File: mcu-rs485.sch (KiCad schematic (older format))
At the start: 10 parts

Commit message: Initial PCB routed
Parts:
- removed U?: ATmega2560-16AU, Package_QFP:TQFP-100_14x14mm_P0.5mm, symbol MCU_Microchip_ATmega:ATmega2560-16AU
- added C46, C8: 100uF, Capacitor_SMD:CP_Elec_6.3x5.4, symbol Device:CP
- added C47, C53, C54, C55: 100nF, Capacitor_SMD:C_0603_1608Metric_Pad1.08x0.95mm_HandSolder, symbol Device:C_Small
- added F1: Fuse, Fuse:Fuse_1206_3216Metric_Pad1.42x1.75mm_HandSolder, symbol Device:Fuse
- added U10, U11, U12: MCP23S17_SS, Package_SO:SSOP-28_5.3x10.2mm_P0.65mm, symbol Interface_Expansion:MCP23S17_SS
- added U6: TSOP382xx, OptoDevice:Vishay_MINICAST-3Pin, symbol Interface_Optical:TSOP382xx
- added U9: ATmega328PB-AU, Package_QFP:TQFP-32_7x7mm_P0.8mm, symbol MCU_Microchip_ATmega:ATmega328PB-AU
- C48, C51, C52: renamed from C?; footprint (none) -> Capacitor_SMD:C_0603_1608Metric_Pad1.08x0.95mm_HandSolder
- C49, C50: renamed from C?; footprint (none) -> Capacitor_SMD:C_0805_2012Metric_Pad1.18x1.45mm_HandSolder
- J1: renamed from J?; footprint (none) -> Connector_Dsub:DSUB-9_Female_Horizontal_P2.77x2.84mm_EdgePinOffset9.90mm_Housed_MountingHolesOffset11.32mm
- R53: renamed from R?; footprint (none) -> Resistor_SMD:R_0603_1608Metric_Pad0.98x0.95mm_HandSolder
- U8: renamed from U?; footprint (none) -> Package_SO:SO-8_5.3x6.2mm_P1.27mm
- Y1: renamed from Y?; footprint (none) -> Crystal:Resonator_SMD_muRata_CSTxExxV-3Pin_3.0x1.1mm_HandSoldering
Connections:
- net labels added: IR_OUT, MISO, MOSI, SCK, SS0, SS1, SS2
- wire segments 34 -> 43
- no-connect marks 2 -> 8
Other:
- moved on the sheet: C49, C50, C51, C52, Y1

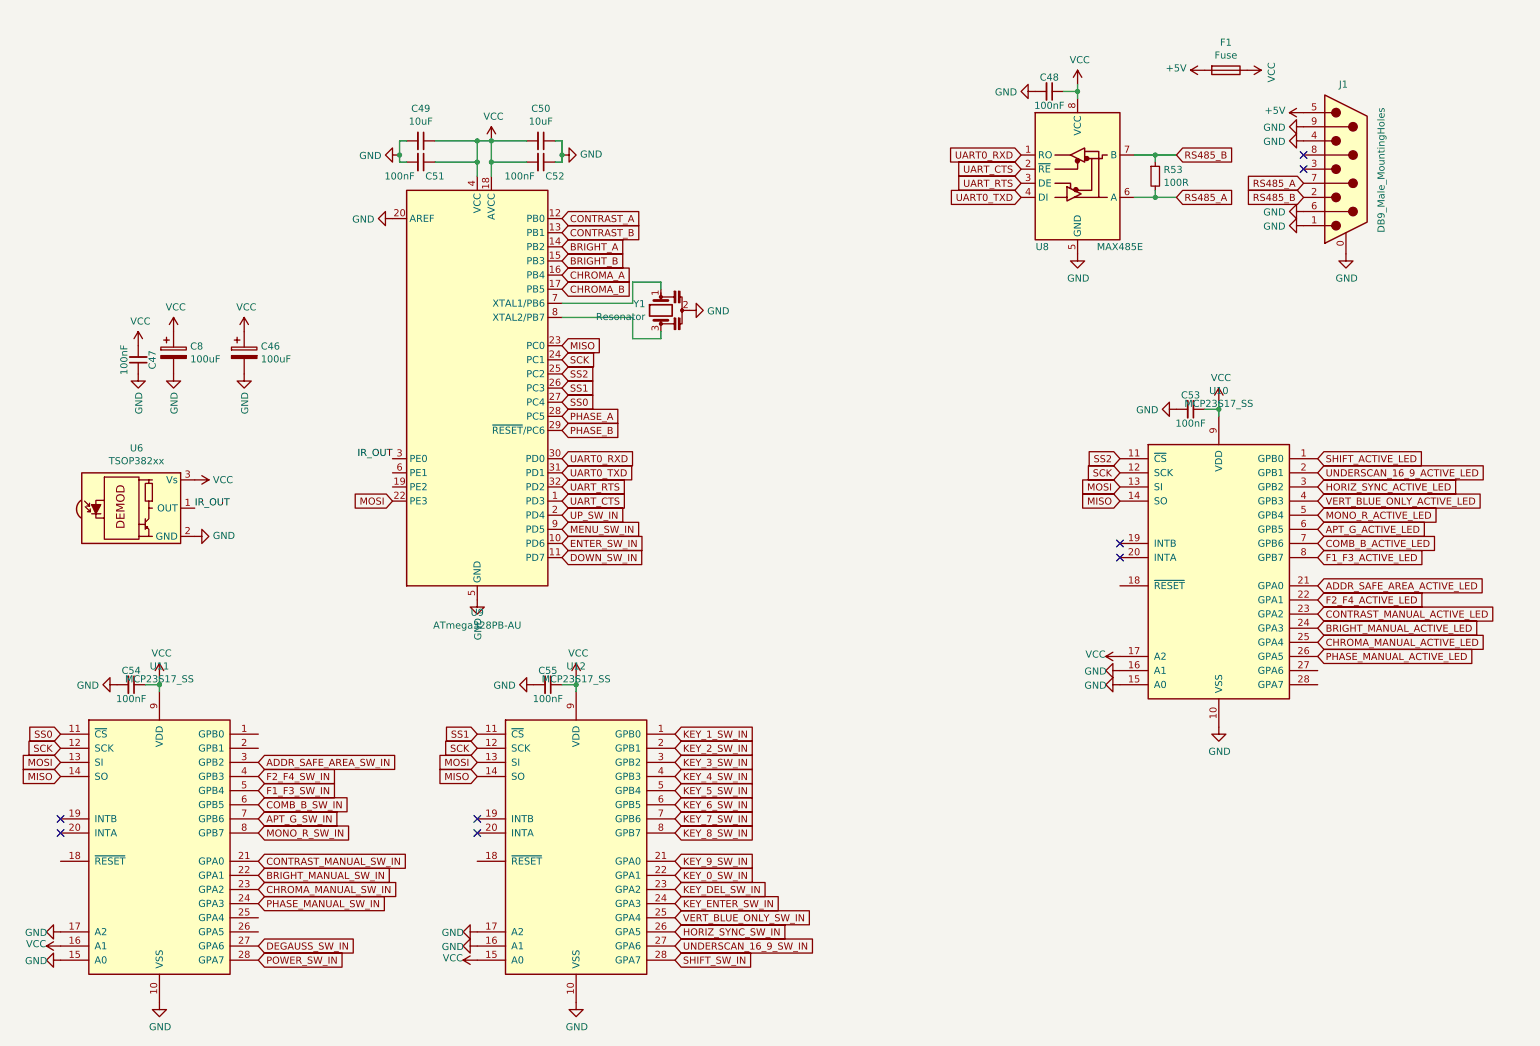
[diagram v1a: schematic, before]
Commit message: Added texts, fixed pullups
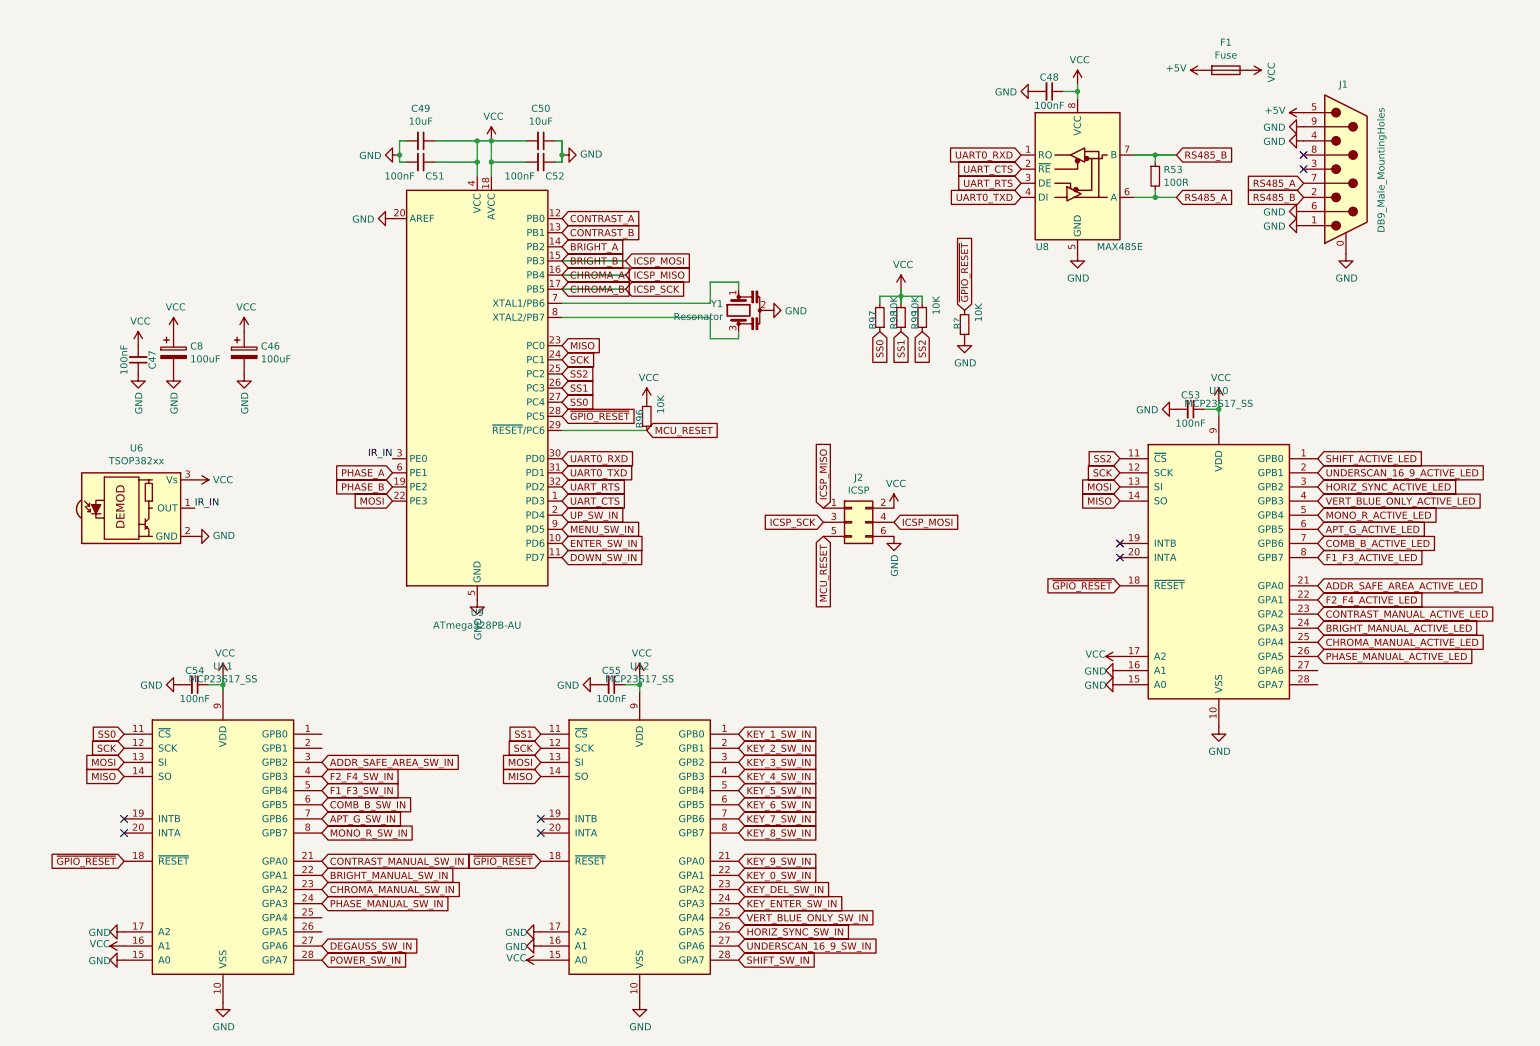
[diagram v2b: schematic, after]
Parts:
- added J2: ICSP, Connector_PinHeader_2.54mm:PinHeader_2x03_P2.54mm_Vertical, symbol Connector_Generic:Conn_02x03_Odd_Even
- added R96, R97, R98, R99, R?: 10K, Resistor_SMD:R_0603_1608Metric_Pad0.98x0.95mm_HandSolder, symbol Device:R_Small
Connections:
- net BRIGHT_B: now also J2.4 (Pin_4)
- net CHROMA_A: now also J2.1 (Pin_1)
- net CHROMA_B: now also J2.3 (Pin_3)
- net GND: now also J2.6 (Pin_6), R?.1
- net PHASE_A: now also U9.6 (PE1); no longer U9.28 (PC5)
- net PHASE_B: now also U9.19 (PE2); no longer U9.29 (~RESET~/PC6)
- net SS0: now also R97.1
- net SS1: now also R98.1
- net SS2: now also R99.1
- net VCC: now also J2.2 (Pin_2), R96.2, R97.2, R98.2, R99.2
- net ~GPIO_RESET: now reaches U11.18 (~RESET~)
- net ~GPIO_RESET: now also U10.18 (~RESET~), U12.18 (~RESET~), U9.28 (PC5), R?.2
- net IR_OUT renamed IR_IN
- new net MCU_RESET: J2.5 (Pin_5), R96.1, U9.29 (~RESET~/PC6)
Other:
- moved on the sheet: C54, C55, U11, U12, Y1

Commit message: Minor changes
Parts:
- gave numbers to parts that had none: 1
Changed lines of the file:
@@
 ~GPIO_RESET
 $Comp
-L Device:R_Small R?
+L Device:R_Small R100
 U 1 1 61976433
 P 7250 2650
-F 0 "R?" V 7300 2600 50  0000 L CNN
+F 0 "R100" V 7300 2600 50  0000 L CNN
 F 1 "10K" V 7150 2500 50  0000 L CNN
 F 2 "Resistor_SMD:R_0603_1608Metric_Pad0.98x0.95mm_HandSolder" H 7250 2650 50  0001 C CNN
@@
 $EndComp
 $Comp
-L power:GND #PWR?
+L power:GND #PWR0312
 U 1 1 6197A8DF
 P 7250 2750
-F 0 "#PWR?" H 7250 2500 50  0001 C CNN
+F 0 "#PWR0312" H 7250 2500 50  0001 C CNN
 F 1 "GND" H 7255 2577 50  0000 C CNN
 F 2 "" H 7250 2750 50  0001 C CNN

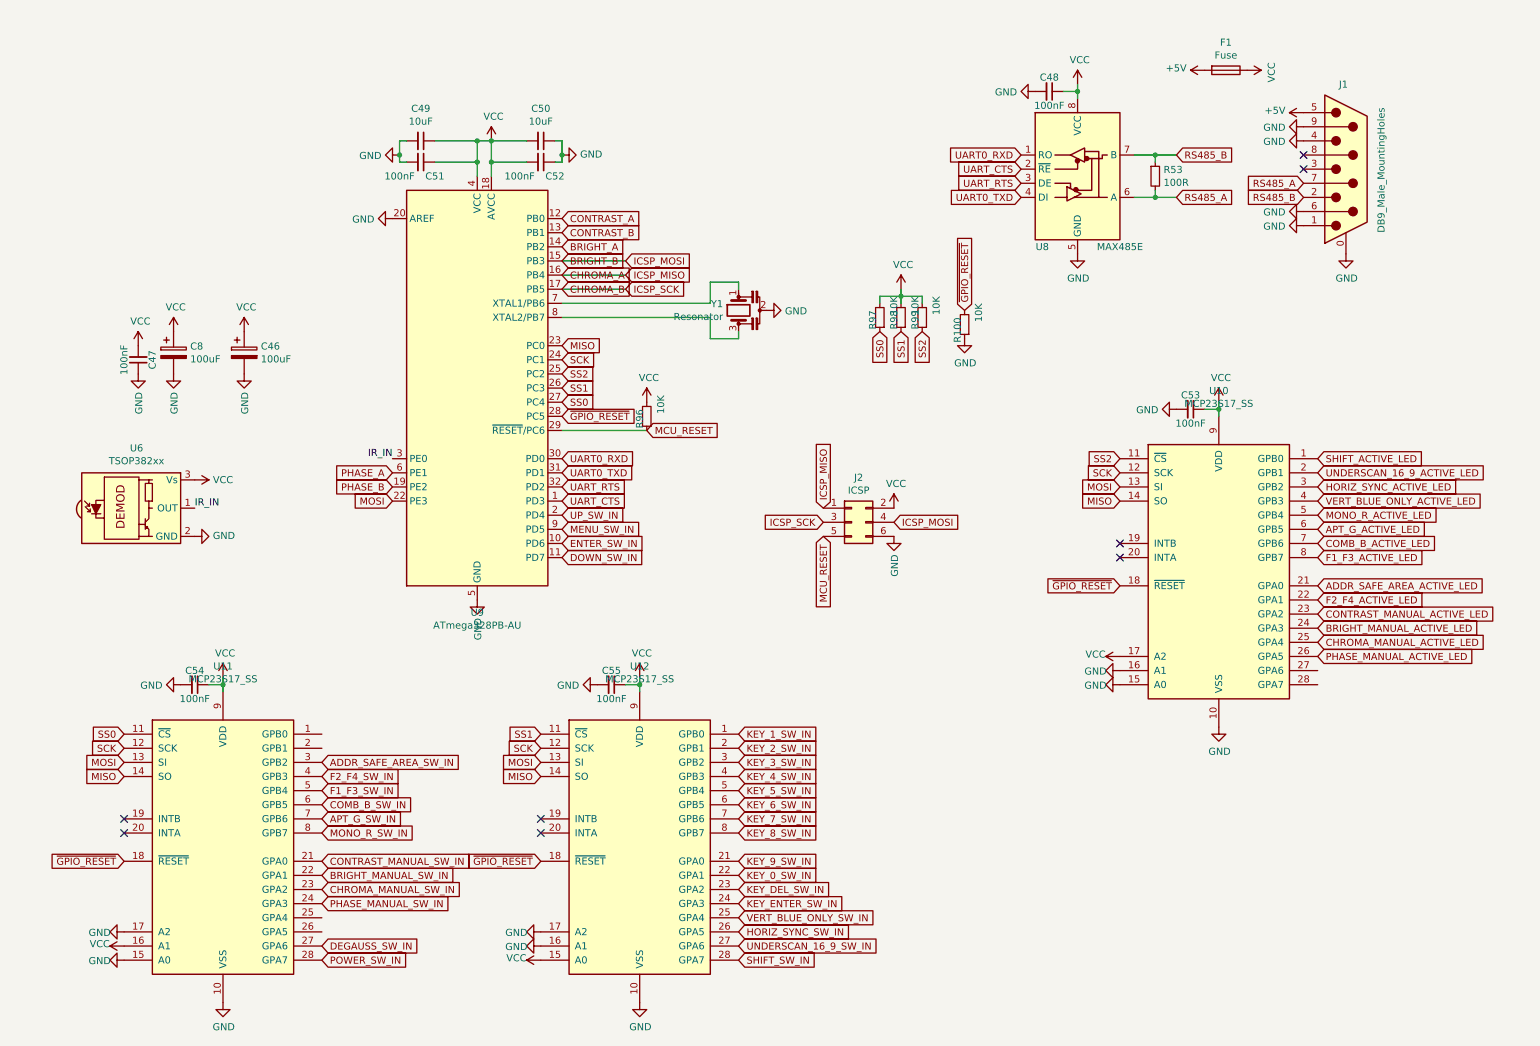
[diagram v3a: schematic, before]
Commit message: A bunch of changes, full duplex 422
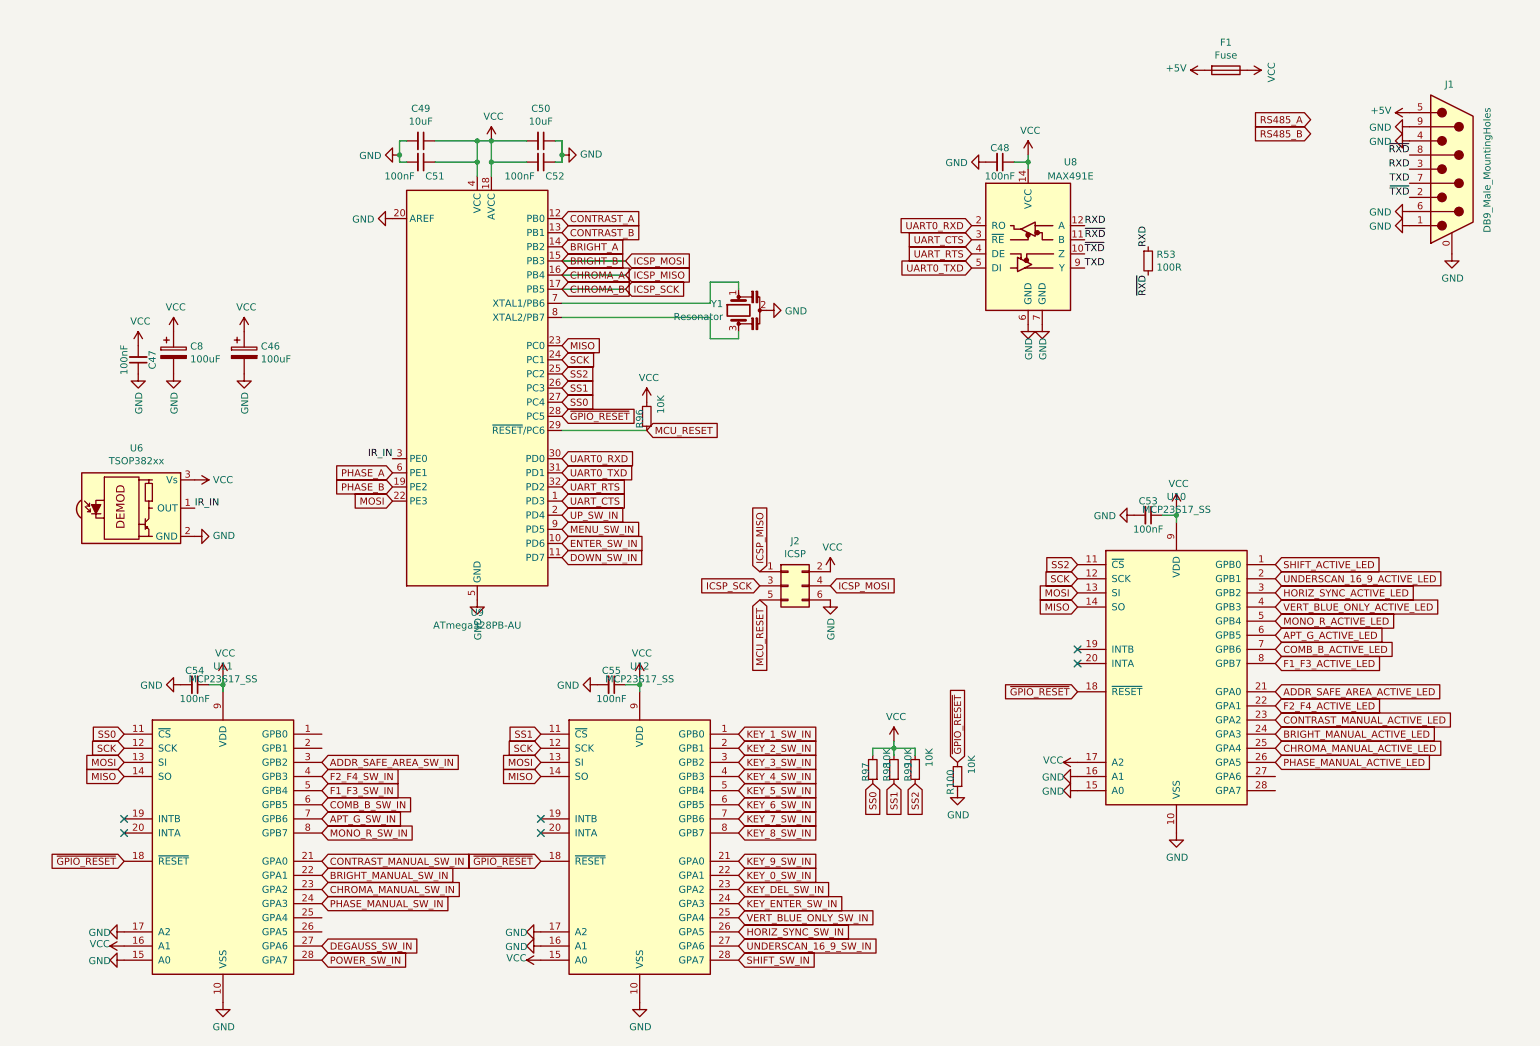
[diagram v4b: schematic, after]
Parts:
- removed U8: MAX485E, Package_SO:SO-8_5.3x6.2mm_P1.27mm, symbol Interface_UART:MAX485E
- added U8: MAX491E, Package_SO:SOIC-14_3.9x8.7mm_P1.27mm, symbol Interface_UART:MAX491E
- J1: footprint Connector_Dsub:DSUB-9_Female_Horizontal_P2.77x2.84mm_EdgePinOffset9.90mm_Housed_MountingHolesOffset11.32mm -> Connector_Dsub:DSUB-9_Female_Horizontal_P2.77x2.84mm_EdgePinOffset7.70mm_Housed_MountingHolesOffset9.12mm
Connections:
- net GND: now also U8.6 (GND), U8.7 (GND)
- net RS485_A: no longer J1.7, R53.2
- net RS485_B: no longer J1.2, R53.1
- net UART0_RXD: now also U8.2 (RO)
- net UART0_TXD: now also U8.5 (DI)
- net UART_CTS: now also U8.3 (~RE)
- net UART_RTS: now also U8.4 (DE)
- net VCC: now also U8.14 (VCC)
- net RXD: now reaches J1.3
- net RXD: now also R53.1, U8.12 (A)
- net ~RXD: now reaches J1.8
- net ~RXD: now also R53.2, U8.11 (B)
- new net TXD: J1.7, U8.9 (Y)
- new net ~TXD: J1.2, U8.10 (Z)
- no-connect marks 8 -> 6
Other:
- moved on the sheet: C48, C53, J1, J2, R100, R97, R98, R99, U10

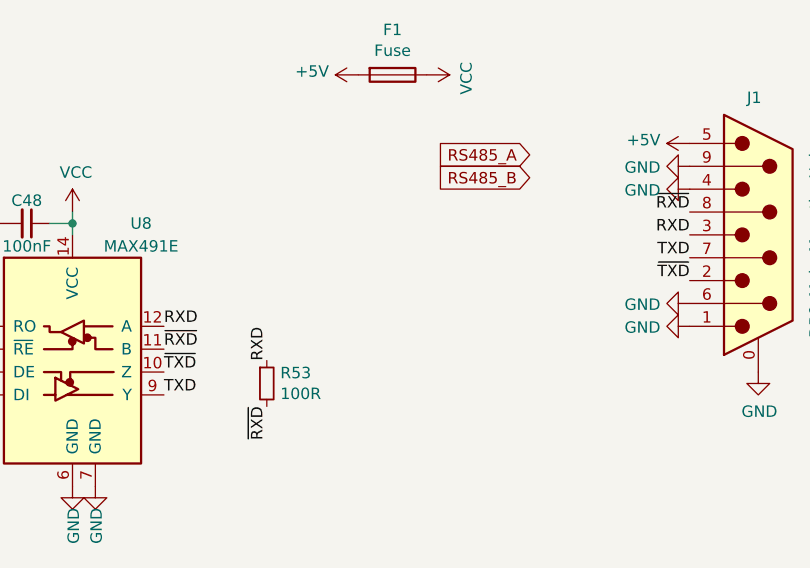
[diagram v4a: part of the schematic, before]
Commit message: Fixed switch footprints and encoder resistors
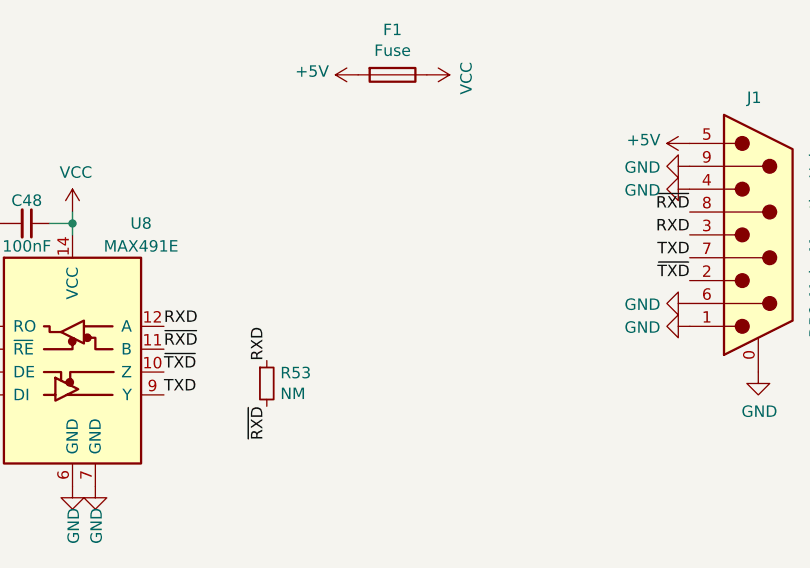
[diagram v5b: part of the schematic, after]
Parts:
- R53: value 100R -> NM
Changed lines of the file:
@@
 	0    -1   -1   0
 $EndComp
-Text GLabel 9700 1200 0    50   Input ~ 0
-RS485_A
-Text GLabel 9700 1300 0    50   Input ~ 0
-RS485_B
 Text GLabel 9450 5350 2    50   Input ~ 0
 F2_F4_ACTIVE_LED
@@
 P 8550 2200
 F 0 "R53" H 8609 2246 50  0000 L CNN
-F 1 "100R" H 8609 2155 50  0000 L CNN
+F 1 "NM" H 8609 2155 50  0000 L CNN
 F 2 "Resistor_SMD:R_0603_1608Metric_Pad0.98x0.95mm_HandSolder" H 8550 2200 50  0001 C CNN
 F 3 "~" H 8550 2200 50  0001 C CNN

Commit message: Initial revision B
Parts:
- removed R99: 10K, Resistor_SMD:R_0603_1608Metric_Pad0.98x0.95mm_HandSolder, symbol Device:R_Small
- added C56, C57: 10uF, Capacitor_SMD:C_0805_2012Metric_Pad1.18x1.45mm_HandSolder, symbol Device:C_Small
- added C58, C59: 100nF, Capacitor_SMD:C_0603_1608Metric_Pad1.08x0.95mm_HandSolder, symbol Device:C_Small
- added J3: Micro_SD_Card_Det, MEM2061:MEM2061, symbol Connector:Micro_SD_Card_Det
- added J4: Conn_01x05_Male, Connector_PinHeader_2.54mm:PinHeader_1x05_P2.54mm_Vertical, symbol Connector:Conn_01x05_Male
- added U21: NCP1117-3.3_SOT223, Package_TO_SOT_SMD:SOT-223-3_TabPin2, symbol Regulator_Linear:NCP1117-3.3_SOT223
- added U22: 74LVC125, Package_SO:TSSOP-14_4.4x5mm_P0.65mm, symbol 74xx:74LVC125
- R53: value NM -> 1K
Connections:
- net SS2 is gone; now on net SS0: U10.11 (~CS~), U9.25 (PC2)
- net BRIGHT_A: now also U9.10 (PD6); no longer U9.14 (PB2)
- net BRIGHT_B: now also U9.9 (PD5); no longer J2.4 (Pin_4), U9.15 (PB3)
- net CHROMA_A: now also U9.26 (PC3); no longer J2.1 (Pin_1), U9.16 (PB4)
- net CHROMA_B: now also U9.27 (PC4); no longer J2.3 (Pin_3), U9.17 (PB5)
- net DOWN_SW_IN: now also U11.1 (GPB0); no longer U9.11 (PD7)
- net ENTER_SW_IN: now also U11.2 (GPB1); no longer U9.10 (PD6)
- net GND: now also U8.3 (~RE), C56.1, C57.1, C58.1, C59.1, J3.11 (SHIELD), J3.4 (VDD), J4.5 (Pin_5), U21.1 (GND), U22.1, U22.10, U22.13, U22.4, U22.7 (GND)
- net MENU_SW_IN: now also U11.26 (GPA5); no longer U9.9 (PD5)
- net PHASE_A: now also U9.32 (PD2); no longer U9.6 (PE1)
- net PHASE_B: now also U9.1 (PD3); no longer U9.19 (PE2)
- net RXD: now also J4.1 (Pin_1); no longer R53.1
- net SS0: now also U12.11 (~CS~); no longer U9.27 (PC4)
- net TXD: now also J4.4 (Pin_4)
- net UP_SW_IN: now also U11.25 (GPA4); no longer U9.2 (PD4)
- net VCC: now also U8.4 (DE), C56.2, U21.3 (VI)
- net ~RXD: now also J4.2 (Pin_2); no longer R53.2
- net ~TXD: now also J4.3 (Pin_3)
- removed net SS1: R98.1, U12.11 (~CS~), U9.26 (PC3)
- removed net UART_CTS: U8.3 (~RE), U9.1 (PD3)
- removed net UART_RTS: U8.4 (DE), U9.32 (PD2)
- new net: R53.1, U22.6
- new net +3V3: C57.2, C58.2, C59.2, J3.6 (VSS), U21.2 (VO), U22.14 (VCC)
- new net ICSP_MISO: J2.1 (Pin_1), R53.2, U9.16 (PB4)
- new net ICSP_MOSI: J2.4 (Pin_4), U22.2, U9.15 (PB3)
- new net ICSP_SCK: J2.3 (Pin_3), U22.9, U9.17 (PB5)
- new net SD_CARD_DET: J3.10 (DET_A), R98.1, U9.11 (PD7)
- new net SD_MISO_LV: J3.7 (DAT0), U22.5
- new net SD_MOSI_LV: J3.3 (CMD), U22.3
- new net SD_SCK_LV: J3.5 (CLK), U22.8
- new net SD_SS: U22.12, U9.14 (PB2)
- new net SD_SS_LV: J3.2 (DAT3/CD), U22.11
- no-connect marks 6 -> 11
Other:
- moved on the sheet: C46, C47, C48, C49, C50, C51, C52, C8, F1, J2, R96, R97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
